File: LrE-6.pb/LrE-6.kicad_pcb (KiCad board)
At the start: 2 copper layers, 100 x 100 mm, 112 parts, among them J1 USB_B_Micro, J2 SM06B-SRSS-TB, Q1 2N7002, SW1 SW_Push_45deg, SW10 SW_Push_45deg, SW11 Rotary_Encoder_Switch, SW12 Rotary_Encoder_Switch, SW13 Rotary_Encoder_Switch, SW14 Rotary_Encoder_Switch, SW15 Rotary_Encoder_Switch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

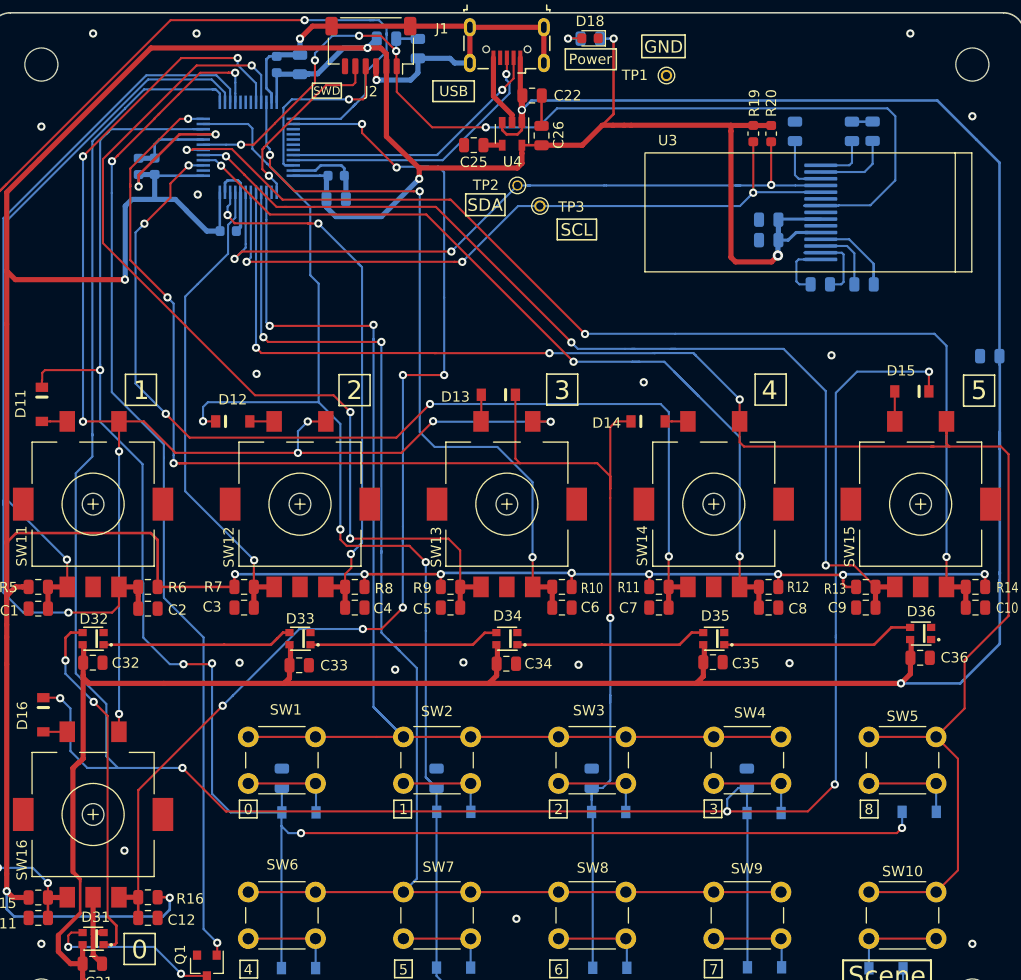
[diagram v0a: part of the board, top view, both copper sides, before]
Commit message: 0.28-6
change Rotary Encoder from 9.5KQ to 'symmetry hole' model.
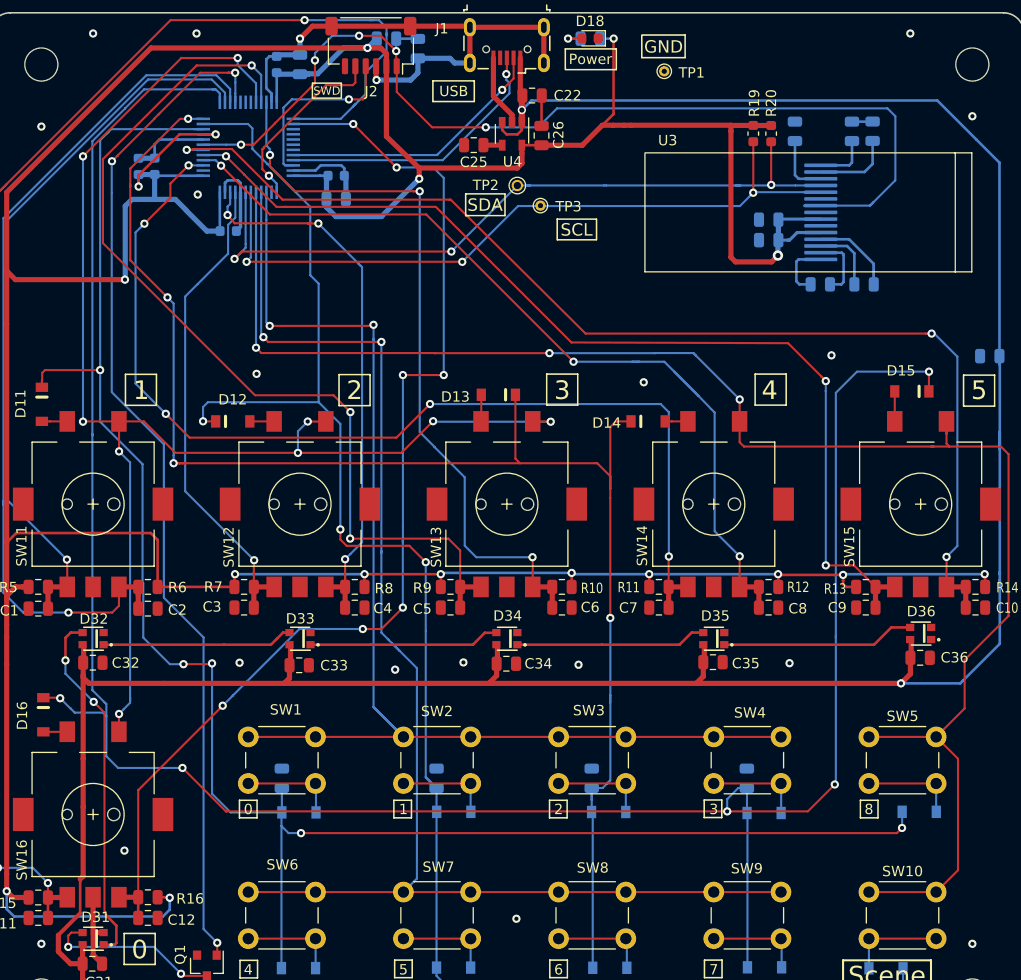
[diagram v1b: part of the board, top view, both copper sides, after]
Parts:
- removed the TP2 at (116.0, 71.7)
- added TP1: TestPoint, TestPoint:TestPoint_THTPad_D1.0mm_Drill0.5mm, F.Cu at (130.2, 60.7)
- SW11, SW12, SW13, SW14, SW15, SW16: footprint LrE-6:RotaryEncoder_EC11E-SMD -> LrE-6:RotaryEncoder_EC11E-SMD2
- TP3: footprint TestPoint:TestPoint_THTPad_D2.0mm_Drill1.0mm -> TestPoint:TestPoint_THTPad_D1.0mm_Drill0.5mm
- moved TP2 17.9 mm to (116.0, 71.7)
- moved TP3 0.07 mm to (118.2, 73.6)
- renumbered TP1 to TP2
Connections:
- D36 pad 1: Net-(D36-Pad1) -> (no net)
- J1 pad 4: Net-(J1-Pad4) -> (no net)
- J2 pad 6: Net-(J2-Pad6) -> (no net)
- TP2 pad 1: GND -> /SDA
- U1 pad 17: Net-(U1-Pad17) -> (no net)
- U1 pad 18: Net-(U1-Pad18) -> (no net)
- U1 pad 19: Net-(U1-Pad19) -> (no net)
- U1 pad 2: Net-(U1-Pad2) -> (no net)
- U1 pad 27: Net-(U1-Pad27) -> (no net)
- U1 pad 28: Net-(U1-Pad28) -> (no net)
- U1 pad 29: Net-(U1-Pad29) -> (no net)
- U1 pad 30: Net-(U1-Pad30) -> (no net)
- U1 pad 31: Net-(U1-Pad31) -> (no net)
- U1 pad 38: Net-(U1-Pad38) -> (no net)
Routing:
- net /M3: track 234.7 -> 227.8 mm
- net /ENC0-B: track 111.4 -> 109.5 mm
- net Net-(C23-Pad1): track 7.94 -> 6.34 mm
- net +3V3: track 423.1 -> 424.4 mm
- net /L3: track 134.3 -> 135.5 mm
- net /VBUS: track 266.5 -> 265.8 mm
- net /ENC5-B: track 110.2 -> 110.7 mm

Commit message: 0.28-7
F2.2 PCB ordered.
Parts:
- TP2: footprint TestPoint:TestPoint_THTPad_D2.0mm_Drill1.0mm -> TestPoint:TestPoint_THTPad_D1.0mm_Drill0.5mm
- moved C29 6.35 mm to (144.0, 67.0)
- moved C23 5.75 mm to (151.0, 82.0)
- moved C24 5.03 mm to (154.5, 82.0)
- moved C20 4.11 mm to (144.4, 77.3)
- moved C27 4.09 mm to (144.4, 74.7)
- moved D15 3.30 mm to (150.8, 91.6), turned to 0 degrees
- moved C28 2.44 mm to (146.0, 67.0)
- moved D12 2.23 mm to (90.0, 92.8), turned to 270 degrees
- moved R18 0.94 mm to (142.1, 67.0)
- moved TP3 0.18 mm to (118.2, 73.5)
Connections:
- D36 pad 1: (no net) -> Net-(D36-Pad1)
- J1 pad 4: (no net) -> Net-(J1-Pad4)
- J2 pad 6: (no net) -> Net-(J2-Pad6)
- U1 pad 17: (no net) -> Net-(U1-Pad17)
- U1 pad 18: (no net) -> Net-(U1-Pad18)
- U1 pad 19: (no net) -> Net-(U1-Pad19)
- U1 pad 2: (no net) -> Net-(U1-Pad2)
- U1 pad 27: (no net) -> Net-(U1-Pad27)
- U1 pad 28: (no net) -> Net-(U1-Pad28)
- U1 pad 29: (no net) -> Net-(U1-Pad29)
- U1 pad 30: (no net) -> Net-(U1-Pad30)
- U1 pad 31: (no net) -> Net-(U1-Pad31)
- U1 pad 38: (no net) -> Net-(U1-Pad38)
- U3 pad 10: GND -> /SCL
- U3 pad 11: /SCL -> /SDA
- U3 pad 12: /SDA -> Net-(R18-Pad1)
- U3 pad 13: Net-(R18-Pad1) -> Net-(C29-Pad2)
- U3 pad 14: Net-(C29-Pad2) -> Net-(C28-Pad2)
- U3 pad 6: GND -> Net-(U3-Pad6)
- U3 pad 7: +3V3 -> GND
- U3 pad 8: GND -> +3V3
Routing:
- net /M3: track 227.8 -> 219.2 mm
- net /M1: track 162.0 -> 154.3 mm
- net /ENC4-A: track 102.2 -> 95.6 mm
- net /M2: track 149.6 -> 153.9 mm
- net Net-(R18-Pad1): track 5.93 -> 10.1 mm
- net +3V3: track 424.4 -> 420.6 mm, vias 17 -> 18
- net /ENC5-A: track 96.8 -> 100.6 mm
- net /NRST: track 99.9 -> 96.2 mm
- net /ENC2-A: track 46.9 -> 43.5 mm
- net /SCL: track 71.7 -> 74.7 mm
- net /L3: track 135.5 -> 132.9 mm, vias 9 -> 7
- net GND: track 96.1 -> 98.7 mm, vias 20 -> 37
- net /ENC0-A: track 137.7 -> 135.4 mm
- net /ENC3-A: track 92.1 -> 94.3 mm
- net Net-(C24-Pad2): track 5.80 -> 7.88 mm
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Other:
- outline, holes or cut-outs redrawn

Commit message: 0.32
F2.2 PB first run
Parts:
- R19, R20: footprint Resistor_SMD:R_0603_1608Metric -> Resistor_SMD:R_0805_2012Metric
- moved C27 2.11 mm to (146.5, 74.7)
- moved C20 2.09 mm to (146.5, 77.3)
- moved C24 2.06 mm to (156.5, 81.5)
- moved C23 1.82 mm to (149.2, 81.5), turned to 0 degrees
- moved R19 0.22 mm to (138.6, 66.7)
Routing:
- net +3V3: track 420.6 -> 425.2 mm
- net Net-(C28-Pad2): track 6.05 -> 9.17 mm
- net Net-(C29-Pad2): track 8.02 -> 11.0 mm
- net Net-(R18-Pad1): track 10.1 -> 13.1 mm
- net /SCL: track 74.7 -> 77.6 mm
- net Net-(C23-Pad2): track 7.95 -> 5.15 mm
- net /SDA: track 73.4 -> 76.2 mm
- net Net-(C24-Pad2): track 7.88 -> 6.40 mm
- net Net-(C24-Pad1): track 10.0 -> 8.84 mm
- net Net-(C23-Pad1): track 5.95 -> 6.67 mm
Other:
- board text added: "F2.4"
- board text removed: "F2.2"

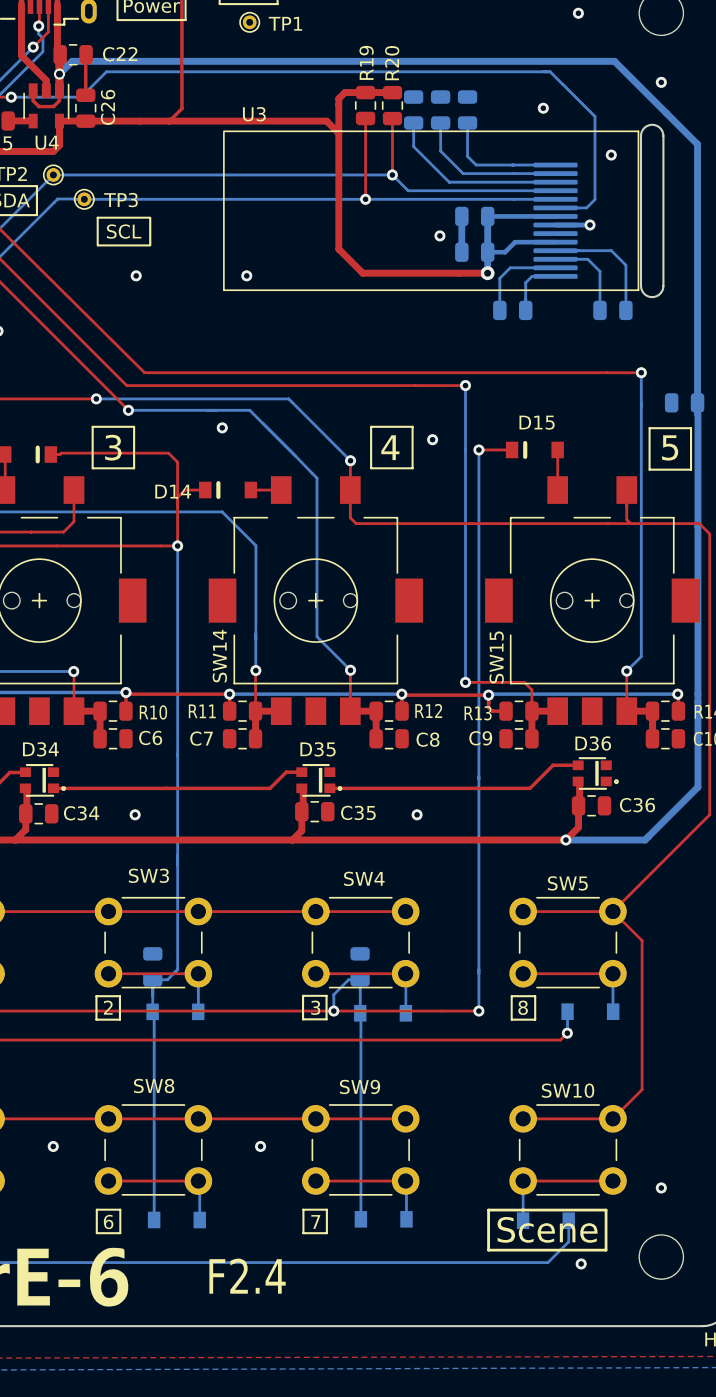
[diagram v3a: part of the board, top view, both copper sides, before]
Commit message: 0.32-1
Fixed SSD1306 Horizontal paging initialize
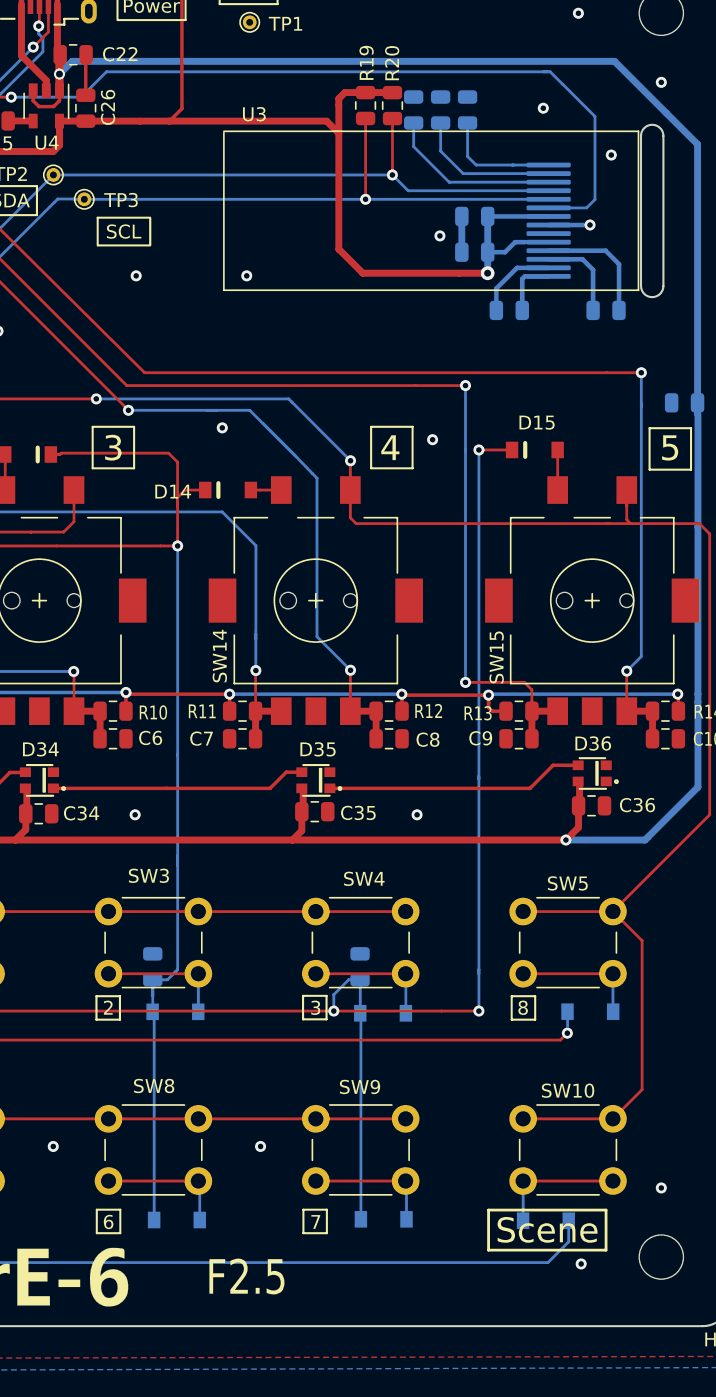
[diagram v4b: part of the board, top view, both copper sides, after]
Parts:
- moved C24 0.50 mm to (156.0, 81.5)
- moved C23 0.25 mm to (149.0, 81.5)
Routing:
- net +3V3: track 425.2 -> 424.2 mm
- net Net-(C23-Pad2): track 5.15 -> 5.96 mm
- net Net-(C23-Pad1): track 6.67 -> 5.99 mm
- net Net-(R18-Pad1): track 13.1 -> 12.6 mm
- net Net-(C29-Pad2): track 11.0 -> 10.5 mm
- net Net-(C28-Pad2): track 9.17 -> 8.67 mm
- net GND: track 99.2 -> 99.7 mm
- net /SDA: track 76.2 -> 75.7 mm
- net /SCL: track 77.6 -> 77.1 mm
- net /NRST: track 96.6 -> 97.1 mm
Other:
- board text added: "F2.5"
- board text removed: "F2.4"

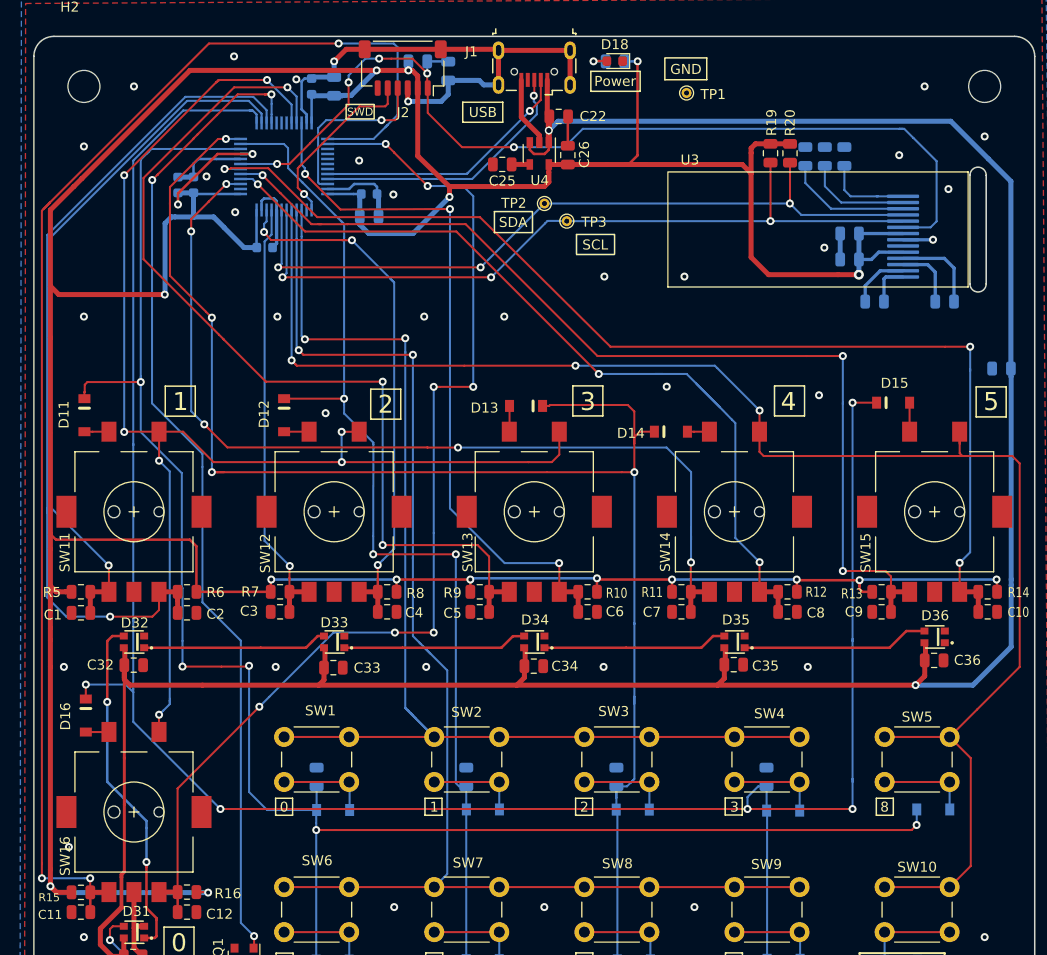
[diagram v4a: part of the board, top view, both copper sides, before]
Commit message: 0.33-1
modify EC11/9.5KQ structure.
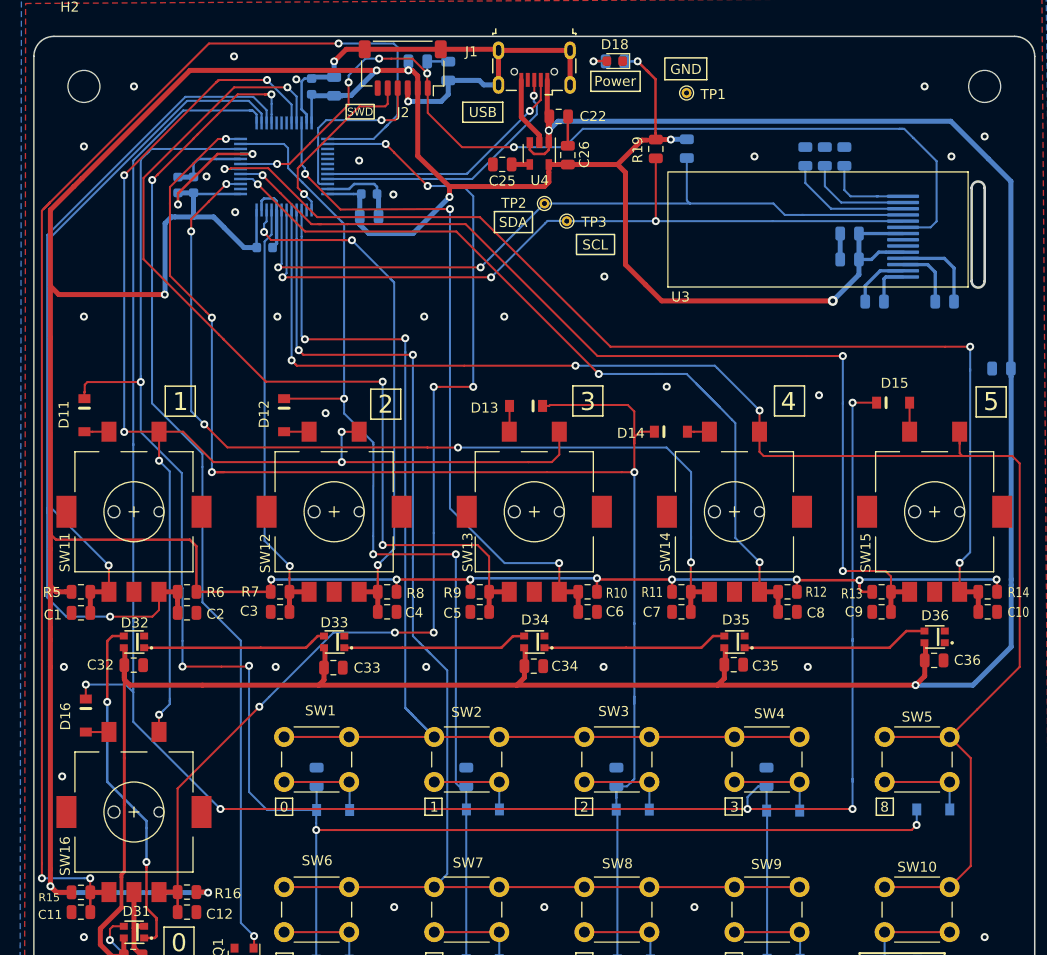
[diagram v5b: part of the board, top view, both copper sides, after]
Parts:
- R20: moved to B.Cu
- moved R19 11.5 mm to (127.1, 66.2)
- moved R20 10.3 mm to (130.2, 66.2)
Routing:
- net GND: track 99.7 -> 96.7 mm, vias 37 -> 34
- net +3V3: track 424.2 -> 426.7 mm, vias 18 -> 19
- net /SDA: track 75.7 -> 76.3 mm, vias 3 -> 2
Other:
- outline, holes or cut-outs redrawn

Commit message: 0.33-5
F2.8 board
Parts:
- removed TP2, TP3: TestPoint-Connector, TestPoint:TestPoint_THTPad_D1.0mm_Drill0.5mm
- R24: moved to F.Cu
- moved D18 66.5 mm to (105.0, 121.5), turned to 90 degrees
- moved R24 66.1 mm to (107.1, 121.7), turned to 90 degrees
- moved TP1 57.8 mm to (166.0, 106.0)
- moved D13 57.0 mm to (149.2, 136.9)
- moved C26 57.0 mm to (153.4, 111.9)
- moved C4 57.0 mm to (135.3, 157.5)
- moved C5 57.0 mm to (144.6, 157.5)
- moved D3 57.0 mm to (159.8, 177.3)
- moved D6 57.0 mm to (129.9, 192.3)
- moved J2 57.0 mm to (136.9, 103.2)
- moved R8 57.0 mm to (135.3, 155.5)
- moved R9 57.0 mm to (144.6, 155.5)
- moved C21 57.0 mm to (141.4, 103.5)
- moved D16 57.0 mm to (105.2, 167.9)
- moved C1 57.0 mm to (104.7, 157.6)
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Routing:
- net GND: track 96.7 -> 112.0 mm, vias 34 -> 63
- net +3V3: track 426.7 -> 421.1 mm, vias 19 -> 18
- net Net-(D18-Pad2): track 2.56 -> 2.11 mm, vias 1 -> 0
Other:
- board text added: "F2.8"
- board text removed: "F2.5"
- board text removed: "SCL"
- board text removed: "SDA"
